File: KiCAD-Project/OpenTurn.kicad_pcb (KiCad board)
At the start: 4 copper layers, 66 x 84.5 mm, 146 parts, among them J201 XT30, J202 Conn_02x04_Odd_Even, J203 Conn_01x03_Shielded, J204 Conn_01x03_Shielded, J301 GPIOs, J302 JTAG/SWD, J303 Conn_01x03_Shielded, Q501 IAUC120N06S5N017ATMA1, Q502 IAUC120N06S5N017ATMA1, Q601 IAUC120N06S5N017ATMA1, Q602 IAUC120N06S5N017ATMA1, Q701 IAUC120N06S5N017ATMA1, Q702 IAUC120N06S5N017ATMA1, U201 TI_TCAN337G, U202 TLE5012B_E1000, U203 MAX15062A, U301 CY8C6244AZI-S4D92, U302 MCP9700AT-HTT, U401 DRV8323SRTAR-DRV8323SRTAR, Y301 32MHz

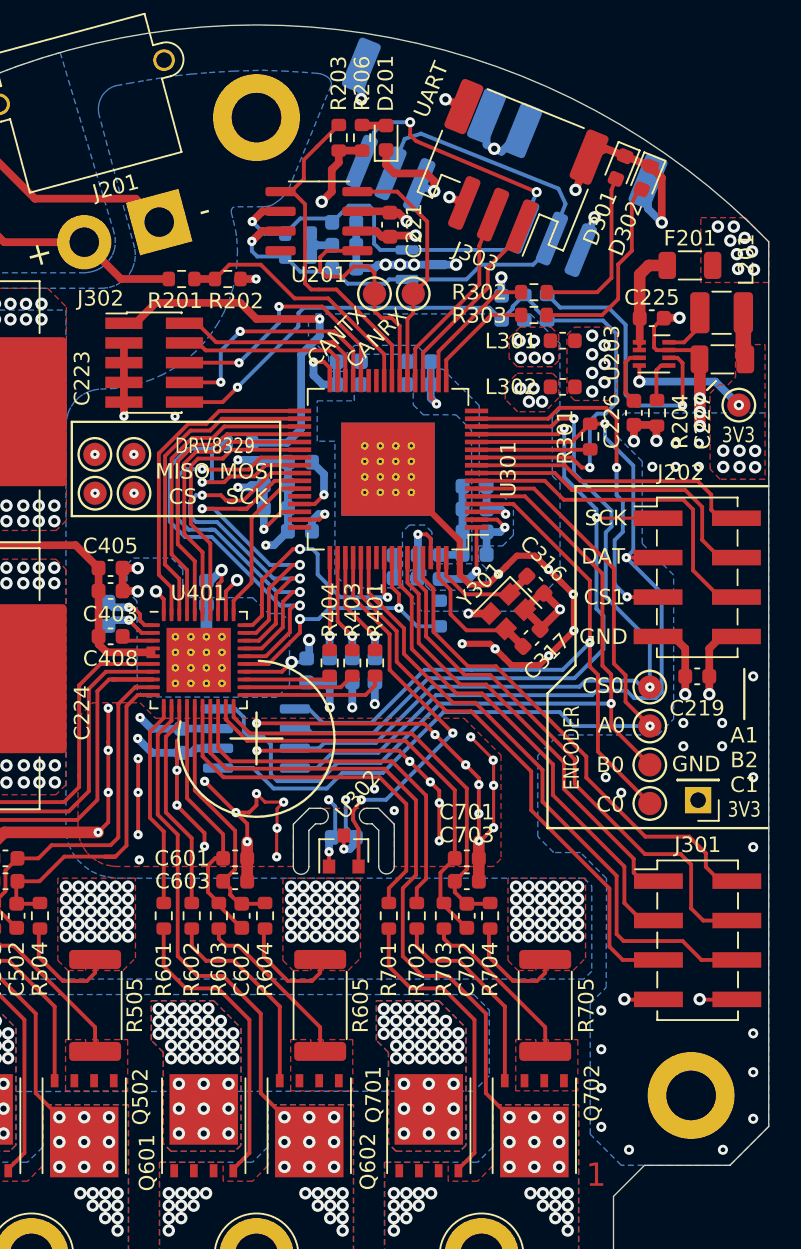
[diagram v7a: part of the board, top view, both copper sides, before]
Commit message: assigned debug UART to different pins
debug UART and DRV SPI used same SCB
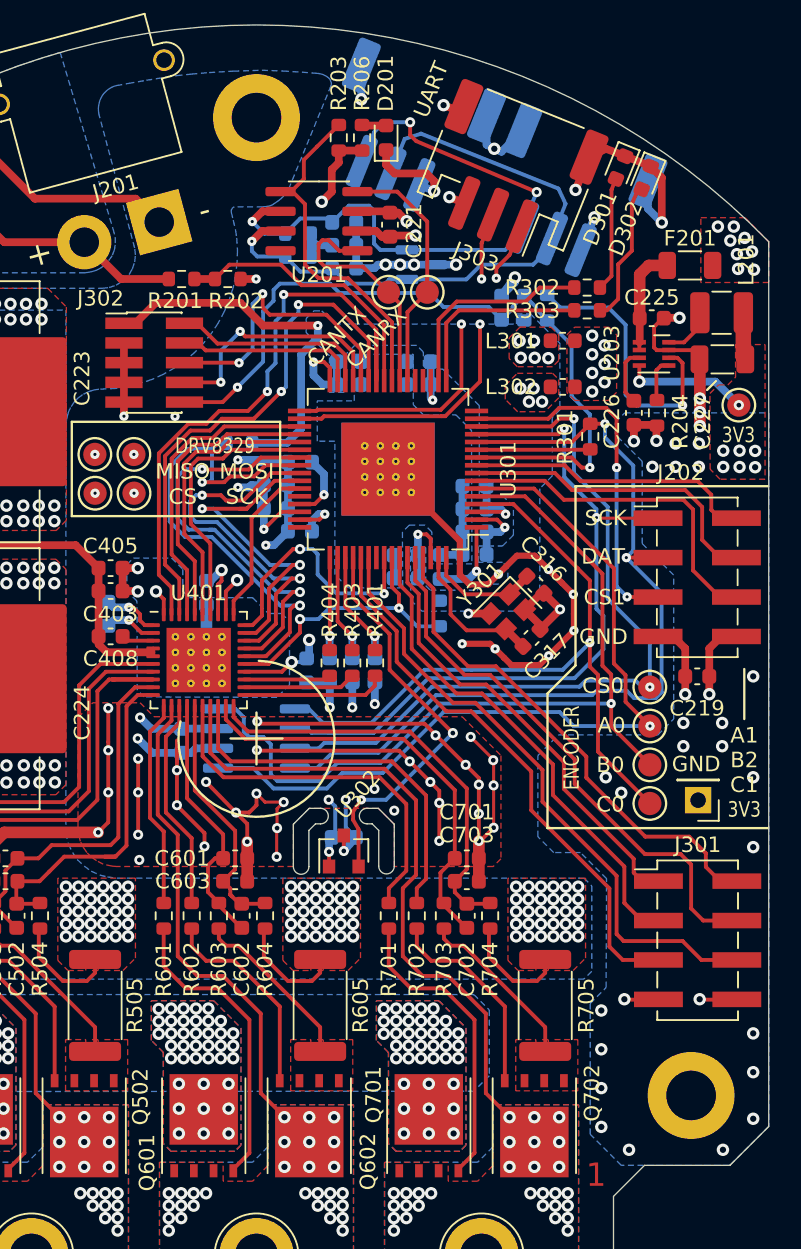
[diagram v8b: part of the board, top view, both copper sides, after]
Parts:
- moved R302 3.44 mm to (148.3, 98.0)
- moved R303 3.44 mm to (148.3, 99.4)
- moved TP202 0.91 mm to (135.5, 98.2)
- moved TP203 0.91 mm to (138.0, 98.2)
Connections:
- J303 pad 1: /MCU/DEBUG_UART_RX -> /MCU/DEBUG_UART_TX
- J303 pad 2: /MCU/DEBUG_UART_TX -> /MCU/DEBUG_UART_RX
- U301 pad 20: /MCU/DEBUG_UART_RX -> unconnected-(U301-Pad20)
- U301 pad 21: /MCU/DEBUG_UART_TX -> unconnected-(U301-Pad21)
- U301 pad 26: unconnected-(U301-Pad26) -> /MCU/DRV_PWM_AL
- U301 pad 27: unconnected-(U301-Pad27) -> /MCU/DRV_PWM_AH
- U301 pad 33: /MCU/DRV_PWM_AL -> /MCU/DEBUG_UART_RX
- U301 pad 34: /MCU/DRV_PWM_AH -> /MCU/DEBUG_UART_TX
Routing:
- net /MCU/DRV_PWM_AL: track 20.9 -> 39.4 mm, vias 0 -> 2
- net /MCU/DRV_PWM_AH: track 20.3 -> 33.9 mm, vias 0 -> 2
- net /MCU/DEBUG_UART_TX: track 12.6 -> 23.6 mm, vias 0 -> 2
- net /MCU/DEBUG_UART_RX: track 12.6 -> 22.9 mm, vias 0 -> 2
- net /MCU/STATUS_LED0: track 7.36 -> 12.3 mm
- net /MCU/STATUS_LED1: track 8.78 -> 13.5 mm
- net Net-(D301-Pad2): track 11.0 -> 7.36 mm
- net Net-(D302-Pad2): track 12.6 -> 9.05 mm
- net /MCU/SWO: track 16.8 -> 19.0 mm
- net GND: track 306.0 -> 307.9 mm
- net VDD: track 49.8 -> 48.7 mm
- net /Interfaces/V_BUS_SENSE: track 16.7 -> 17.8 mm
- net /Interfaces/RESET: track 50.3 -> 49.6 mm
- net /MCU/DRV_ENABLE: track 17.7 -> 17.0 mm
